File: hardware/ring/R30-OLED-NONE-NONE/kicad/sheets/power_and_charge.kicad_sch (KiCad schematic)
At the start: 0 parts

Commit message: feat(hardware): wire 30deg optical ring power and hub USB interfaces for accessibility pointing, ~$9 ring / ~$5-6 hub BOM
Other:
- note added: "Power-path interface scaffold: regulator, sensing, and charge-gate nets are locked here before component symbols land."
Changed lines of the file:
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@@
   (generator_version "0.1")
   (paper "A4")
+  (text "Power-path interface scaffold: regulator, sensing, and charge-gate nets are locked here before component symbols land."
+    (at 20.32 20.32 0)
+    (effects (font (size 1.27 1.27)))
+  )
+  (hierarchical_label "VREG_3V3"
+    (shape output)
+    (at 187.96 38.1 180)
+    (effects (font (size 1.27 1.27)))
+  )
+  (hierarchical_label "VBAT_SENSE"
+    (shape output)
+    (at 187.96 45.72 180)
+    (effects (font (size 1.27 1.27)))
+  )
+  (hierarchical_label "NTC_SENSE"
+    (shape output)
+    (at 187.96 53.34 180)
+    (effects (font (size 1.27 1.27)))
+  )
+  (hierarchical_label "CHARGE_EN"
+    (shape input)
+    (at 25.4 53.34 0)
+    (effects (font (size 1.27 1.27)))
+  )
   (sheet_instances
     (path "/" (page "1"))

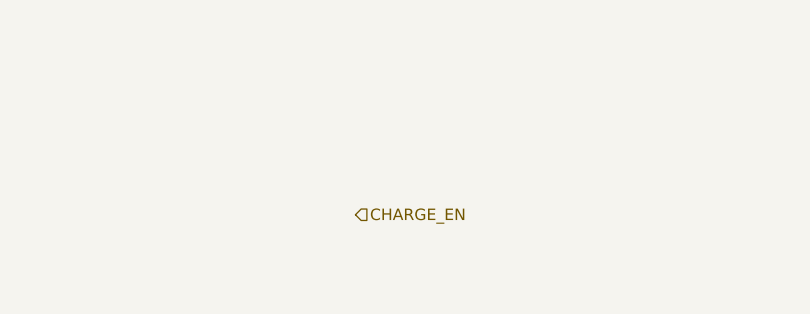
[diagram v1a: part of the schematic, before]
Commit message: feat(hardware): wire 30deg optical ring sensor/click and usb interfaces into top sheet for accessibility pointing, ~$9 ring BOM
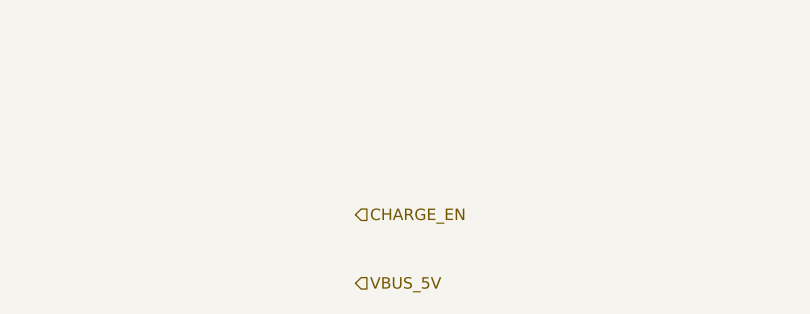
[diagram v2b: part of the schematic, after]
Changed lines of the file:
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@@
+    (effects (font (size 1.27 1.27)))
+  )
+  (hierarchical_label "VBUS_5V"
+    (shape input)
+    (at 25.4 60.96 0)
     (effects (font (size 1.27 1.27)))
   )
